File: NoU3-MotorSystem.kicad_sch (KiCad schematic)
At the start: 38 parts, among them J1 JST SR/SZ, J10 JST SR/SZ, J13 JST SR/SZ, J15 Barrel_Jack, J16 VIN, J17 JST SR/SZ, J18 GND, J4 JST SR/SZ, J7 JST SR/SZ, Q1 AO3401A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

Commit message: updated labels
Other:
- moved on the sheet: TP5
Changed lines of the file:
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@@
 	)
 	(junction
-		(at 72.39 140.97)
+		(at 166.37 40.64)
 		(diameter 0)
 		(color 0 0 0 0)
 	)
 	(junction
-		(at 59.69 171.45)
+		(at 72.39 140.97)
 		(diameter 0)
 		(color 0 0 0 0)
 	)
 	(junction
-		(at 68.58 109.22)
+		(at 59.69 171.45)
 		(diameter 0)
 		(color 0 0 0 0)
 	)
 	(junction
-		(at 166.37 35.56)
+		(at 68.58 109.22)
 		(diameter 0)
 		(color 0 0 0 0)
@@
 	)
 	(junction
-		(at 215.9 36.83)
-		(diameter 0)
-		(color 0 0 0 0)
-	)
-	(junction
 		(at 59.69 116.84)
 		(diameter 0)
@@
 	(wire
 		(pts
-			(xy 215.9 36.83) (xy 224.79 36.83)
-		)
-		(stroke
-			(width 0)
-			(type default)
-		)
-	)
-	(wire
-		(pts
 			(xy 189.23 116.84) (xy 198.12 116.84)
 		)
@@
 	(wire
 		(pts
-			(xy 224.79 35.56) (xy 166.37 35.56)
-		)
-		(stroke
-			(width 0)
-			(type default)
-		)
-	)
-	(wire
-		(pts
 			(xy 186.69 95.25) (xy 186.69 109.22)
 		)
@@
 	(wire
 		(pts
+			(xy 166.37 36.83) (xy 198.12 36.83)
+		)
+		(stroke
+			(width 0)
+			(type default)
+		)
+	)
+	(wire
+		(pts
 			(xy 128.27 104.14) (xy 120.65 104.14)
 		)
@@
 	(wire
 		(pts
-			(xy 181.61 71.12) (xy 181.61 96.52)
+			(xy 166.37 40.64) (xy 166.37 81.28)
 		)
 		(stroke
@@
 	(wire
 		(pts
-			(xy 186.69 116.84) (xy 163.83 116.84)
+			(xy 181.61 71.12) (xy 181.61 96.52)
 		)
 		(stroke
@@
 	(wire
 		(pts
-			(xy 198.12 66.04) (xy 179.07 66.04)
+			(xy 186.69 116.84) (xy 163.83 116.84)
 		)
 		(stroke
@@
 	(wire
 		(pts
-			(xy 191.77 111.76) (xy 191.77 121.92)
+			(xy 198.12 66.04) (xy 179.07 66.04)
 		)
 		(stroke
@@
 	(wire
 		(pts
-			(xy 43.18 124.46) (xy 59.69 124.46)
+			(xy 191.77 111.76) (xy 191.77 121.92)
 		)
 		(stroke
@@
 	(wire
 		(pts
-			(xy 48.26 163.83) (xy 59.69 163.83)
+			(xy 43.18 124.46) (xy 59.69 124.46)
 		)
 		(stroke
@@
 	(wire
 		(pts
-			(xy 166.37 35.56) (xy 166.37 81.28)
+			(xy 48.26 163.83) (xy 59.69 163.83)
 		)
 		(stroke
@@
 	(wire
 		(pts
-			(xy 224.79 36.83) (xy 224.79 35.56)
-		)
-		(stroke
-			(width 0)
-			(type default)
-		)
-	)
-	(wire
-		(pts
 			(xy 143.51 127) (xy 146.05 127)
 		)
@@
 	(wire
 		(pts
-			(xy 198.12 36.83) (xy 215.9 36.83)
+			(xy 48.26 140.97) (xy 59.69 140.97)
 		)
 		(stroke
@@
 	(wire
 		(pts
-			(xy 48.26 140.97) (xy 59.69 140.97)
+			(xy 260.35 124.46) (xy 255.27 124.46)
 		)
 		(stroke
@@
 	(wire
 		(pts
-			(xy 260.35 124.46) (xy 255.27 124.46)
+			(xy 60.96 116.84) (xy 59.69 116.84)
 		)
 		(stroke
@@
 	(wire
 		(pts
-			(xy 60.96 116.84) (xy 59.69 116.84)
+			(xy 85.09 140.97) (xy 90.17 140.97)
 		)
 		(stroke
@@
 	(wire
 		(pts
-			(xy 85.09 140.97) (xy 90.17 140.97)
+			(xy 198.12 31.75) (xy 173.99 31.75)
 		)
 		(stroke
@@
 	(wire
 		(pts
-			(xy 198.12 31.75) (xy 173.99 31.75)
+			(xy 115.57 73.66) (xy 115.57 88.9)
 		)
 		(stroke
@@
 	(wire
 		(pts
-			(xy 115.57 73.66) (xy 115.57 88.9)
+			(xy 166.37 36.83) (xy 166.37 40.64)
 		)
 		(stroke
@@
 	(symbol
 		(lib_id "Connector:TestPoint")
-		(at 166.37 35.56 90)
+		(at 166.37 40.64 90)
 		(unit 1)
 		(exclude_from_sim no)
@@
 		(dnp no)
 		(property "Reference" "TP5"
-			(at 161.29 35.56 90)
+			(at 161.29 40.64 90)
 			(effects
 				(font
@@
 		)
 		(property "Value" "LED0"
-			(at 161.29 33.02 90)
+			(at 161.29 38.1 90)
 			(effects
 				(font
@@
 		)
 		(property "Footprint" "AlfredoFootprints:PogoPad1"
-			(at 166.37 30.48 0)
+			(at 166.37 35.56 0)
 			(effects
 				(font
@@
 		)
 		(property "Datasheet" "~"
-			(at 166.37 30.48 0)
+			(at 166.37 35.56 0)
 			(effects
 				(font
@@
 		)
 		(property "Description" ""
-			(at 166.37 35.56 0)
+			(at 166.37 40.64 0)
 			(effects
 				(font
@@
 		)
 		(property "LCSC" "~"
-			(at 166.37 35.56 0)
+			(at 166.37 40.64 0)
 			(effects
 				(font

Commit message: updated for kicad 9
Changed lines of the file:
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@@
 (kicad_sch
-	(version 20231120)
+	(version 20250114)
 	(generator "eeschema")
-	(generator_version "8.0")
+	(generator_version "9.0")
 	(paper "A4")
+	(text "Power"
+		(exclude_from_sim no)
+		(at 24.13 104.14 0)
+		(effects
+			(font
+				(size 2.54 2.54)
+				(thickness 0.254)
+				(bold yes)
+			)
+			(justify left bottom)
+		)
+	)
+	(text "s"
+		(exclude_from_sim no)
+		(at 63.5 107.95 0)
+		(effects
+			(font
+				(size 1.27 1.27)
+				(bold yes)
+			)
+			(justify left bottom)
+		)
+	)
+	(text "d"
+		(exclude_from_sim no)
+		(at 52.07 107.95 0)
+		(effects
+			(font
+				(size 1.27 1.27)
+				(bold yes)
+			)
+			(justify left bottom)
+		)
+	)
+	(text "g\n"
+		(exclude_from_sim no)
+		(at 55.88 114.3 0)
+		(effects
+			(font
+				(size 1.27 1.27)
+				(bold yes)
+			)
+			(justify left bottom)
+		)
+	)
 	(junction
 		(at 30.48 168.91)
@@
 		)
 	)
-	(text "Power"
-		(exclude_from_sim no)
-		(at 24.13 104.14 0)
-		(effects
-			(font
-				(size 2.54 2.54)
-				(thickness 0.254)
-				(bold yes)
-			)
-			(justify left bottom)
-		)
-	)
-	(text "s"
-		(exclude_from_sim no)
-		(at 63.5 107.95 0)
-		(effects
-			(font
-				(size 1.27 1.27)
-				(bold yes)
-			)
-			(justify left bottom)
-		)
-	)
-	(text "d"
-		(exclude_from_sim no)
-		(at 52.07 107.95 0)
-		(effects
-			(font
-				(size 1.27 1.27)
-				(bold yes)
-			)
-			(justify left bottom)
-		)
-	)
-	(text "g\n"
-		(exclude_from_sim no)
-		(at 55.88 114.3 0)
-		(effects
-			(font
-				(size 1.27 1.27)
-				(bold yes)
-			)
-			(justify left bottom)
-		)
-	)
 	(global_label "E1B"
 		(shape input)
@@
 		(at 198.12 29.21)
 		(size 17.78 20.32)
+		(exclude_from_sim no)
+		(in_bom yes)
+		(on_board yes)
+		(dnp no)
 		(fields_autoplaced yes)
 		(stroke
@@
 		(at 198.12 87.63)
 		(size 17.78 20.32)
+		(exclude_from_sim no)
+		(in_bom yes)
+		(on_board yes)
+		(dnp no)
 		(fields_autoplaced yes)
 		(stroke
@@
 		(at 198.12 114.3)
 		(size 17.78 20.32)
+		(exclude_from_sim no)
+		(in_bom yes)
+		(on_board yes)
+		(dnp no)
 		(fields_autoplaced yes)
 		(stroke
@@
 		(at 198.12 60.96)
 		(size 17.78 20.32)
+		(exclude_from_sim no)
+		(in_bom yes)
+		(on_board yes)
+		(dnp no)
 		(fields_autoplaced yes)
 		(stroke

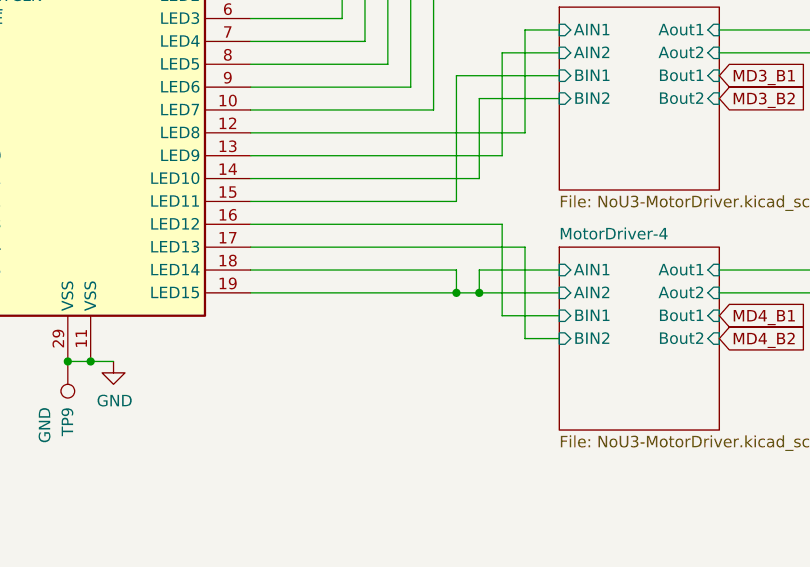
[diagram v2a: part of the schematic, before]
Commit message: Update wiring and remove unused junctions in schematic
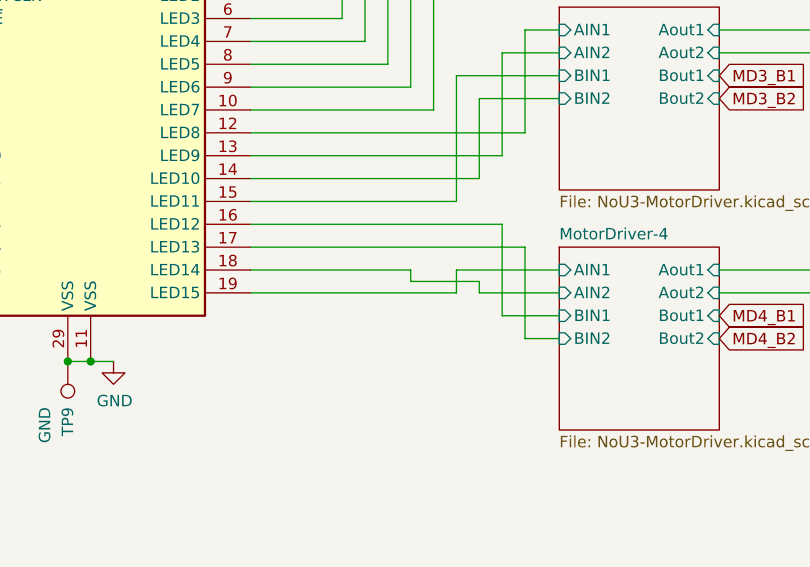
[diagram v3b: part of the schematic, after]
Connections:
- net MotorDriver-4/AIN1: no longer U10.18 (LED14)
- new net MotorDriver-4/AIN2: U10.18 (LED14)
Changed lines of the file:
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@@
-	)
-	(junction
-		(at 186.69 119.38)
-		(diameter 0)
-		(color 0 0 0 0)
 	)
 	(junction
@@
 	)
 	(junction
-		(at 189.23 119.38)
-		(diameter 0)
-		(color 0 0 0 0)
-	)
-	(junction
 		(at 30.48 133.35)
 		(diameter 0)
@@
 	(wire
 		(pts
+			(xy 163.83 116.84) (xy 181.61 116.84)
+		)
+		(stroke
+			(width 0)
+			(type default)
+		)
+	)
+	(wire
+		(pts
 			(xy 215.9 116.84) (xy 232.41 116.84)
 		)
@@
 	(wire
 		(pts
+			(xy 189.23 119.38) (xy 189.23 118.11)
+		)
+		(stroke
+			(width 0)
+			(type default)
+		)
+	)
+	(wire
+		(pts
 			(xy 45.72 106.68) (xy 45.72 109.22)
 		)
@@
 	(wire
 		(pts
-			(xy 189.23 116.84) (xy 198.12 116.84)
-		)
-		(stroke
-			(width 0)
-			(type default)
-		)
-	)
-	(wire
-		(pts
 			(xy 30.48 148.59) (xy 39.37 148.59)
 		)
@@
 	(wire
 		(pts
+			(xy 186.69 116.84) (xy 198.12 116.84)
+		)
+		(stroke
+			(width 0)
+			(type default)
+		)
+	)
+	(wire
+		(pts
 			(xy 59.69 171.45) (xy 62.23 171.45)
 		)
@@
 	(wire
 		(pts
+			(xy 189.23 118.11) (xy 181.61 118.11)
+		)
+		(stroke
+			(width 0)
+			(type default)
+		)
+	)
+	(wire
+		(pts
 			(xy 215.9 90.17) (xy 232.41 90.17)
 		)
@@
 	(wire
 		(pts
+			(xy 163.83 119.38) (xy 186.69 119.38)
+		)
+		(stroke
+			(width 0)
+			(type default)
+		)
+	)
+	(wire
+		(pts
 			(xy 69.85 109.22) (xy 72.39 109.22)
 		)
@@
 	(wire
 		(pts
+			(xy 186.69 119.38) (xy 186.69 116.84)
+		)
+		(stroke
+			(width 0)
+			(type default)
+		)
+	)
+	(wire
+		(pts
 			(xy 229.87 121.92) (xy 232.41 121.92)
 		)
@@
 	(wire
 		(pts
-			(xy 163.83 119.38) (xy 186.69 119.38)
-		)
-		(stroke
-			(width 0)
-			(type default)
-		)
-	)
-	(wire
-		(pts
 			(xy 166.37 36.83) (xy 198.12 36.83)
 		)
@@
 	(wire
 		(pts
-			(xy 186.69 119.38) (xy 186.69 116.84)
-		)
-		(stroke
-			(width 0)
-			(type default)
-		)
-	)
-	(wire
-		(pts
 			(xy 80.01 179.07) (xy 72.39 179.07)
 		)
@@
 	(wire
 		(pts
-			(xy 186.69 116.84) (xy 163.83 116.84)
-		)
-		(stroke
-			(width 0)
-			(type default)
-		)
-	)
-	(wire
-		(pts
 			(xy 198.12 66.04) (xy 179.07 66.04)
 		)
@@
 	(wire
 		(pts
-			(xy 189.23 119.38) (xy 189.23 116.84)
-		)
-		(stroke
-			(width 0)
-			(type default)
-		)
-	)
-	(wire
-		(pts
 			(xy 232.41 41.91) (xy 223.52 41.91)
 		)
@@
 	(wire
 		(pts
+			(xy 181.61 118.11) (xy 181.61 116.84)
+		)
+		(stroke
+			(width 0)
+			(type default)
+		)
+	)
+	(wire
+		(pts
 			(xy 24.13 179.07) (xy 30.48 179.07)
 		)
@@
 		)
 		(stroke
-			(width 0)
-			(type default)
-		)
-	)
-	(wire
-		(pts
-			(xy 186.69 119.38) (xy 189.23 119.38)
-		)
-		(stroke

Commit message: bumped version to NoU3.5
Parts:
- U10: LCSC (none) -> C5191634
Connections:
- net M_ECLK: now reaches TP4.1, U10.22 (EXTCLK)
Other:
- moved on the sheet: TP4
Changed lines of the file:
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@@
 	)
 	(junction
+		(at 110.49 86.36)
+		(diameter 0)
+		(color 0 0 0 0)
+	)
+	(junction
 		(at 30.48 168.91)
 		(diameter 0)
@@
 	(wire
 		(pts
-			(xy 113.03 88.9) (xy 115.57 88.9)
+			(xy 101.6 88.9) (xy 115.57 88.9)
 		)
 		(stroke
@@
 	(wire
 		(pts
+			(xy 110.49 91.44) (xy 110.49 86.36)
+		)
+		(stroke
+			(width 0)
+			(type default)
+		)
+	)
+	(wire
+		(pts
 			(xy 168.91 83.82) (xy 163.83 83.82)
 		)
@@
 	(wire
 		(pts
+			(xy 110.49 86.36) (xy 128.27 86.36)
+		)
+		(stroke
+			(width 0)
+			(type default)
+		)
+	)
+	(wire
+		(pts
 			(xy 215.9 92.71) (xy 232.41 92.71)
 		)
@@
 	(wire
 		(pts
-			(xy 113.03 81.28) (xy 125.73 81.28)
+			(xy 101.6 81.28) (xy 125.73 81.28)
 		)
 		(stroke
@@
 	(wire
 		(pts
+			(xy 101.6 86.36) (xy 110.49 86.36)
+		)
+		(stroke
+			(width 0)
+			(type default)
+		)
+	)
+	(wire
+		(pts
 			(xy 143.51 73.66) (xy 146.05 73.66)
 		)
@@
 	(wire
 		(pts
-			(xy 113.03 83.82) (xy 120.65 83.82)
+			(xy 101.6 83.82) (xy 120.65 83.82)
 		)
 		(stroke
@@
 	(wire
 		(pts
-			(xy 113.03 86.36) (xy 128.27 86.36)
-		)
-		(stroke
-			(width 0)
-			(type default)
-		)
-	)
-	(wire
-		(pts
 			(xy 48.26 171.45) (xy 59.69 171.45)
 		)
@@
 	(global_label "SF_SDA"
 		(shape input)
-		(at 113.03 83.82 180)
+		(at 101.6 83.82 180)
 		(fields_autoplaced yes)
 		(effects
@@
 		)
 		(property "Intersheetrefs" "${INTERSHEET_REFS}"
-			(at 103.9446 83.82 0)
+			(at 92.5146 83.82 0)
 			(effects
 				(font
@@
 	(global_label "SF_SCL"
 		(shape input)
-		(at 113.03 81.28 180)
+		(at 101.6 81.28 180)
 		(fields_autoplaced yes)
 		(effects
@@
 		)
 		(property "Intersheetrefs" "${INTERSHEET_REFS}"
-			(at 104.0051 81.28 0)
+			(at 92.5751 81.28 0)
 			(effects
 				(font
@@
 		)
 	)
+	(global_label "M_ECLK"
+		(shape input)
+		(at 101.6 86.36 180)
+		(fields_autoplaced yes)
+		(effects
+			(font
+				(size 1.27 1.27)
+			)
+			(justify right)
+		)
+		(property "Intersheetrefs" "${INTERSHEET_REFS}"
+			(at 92.1329 86.36 0)
+			(effects
+				(font
+					(size 1.27 1.27)
+				)
+				(justify right)
+				(hide yes)
+			)
+		)
+	)
 	(global_label "M_OE"
 		(shape input)
-		(at 113.03 88.9 180)
+		(at 101.6 88.9 180)
 		(fields_autoplaced yes)
 		(effects
@@
 		)
 		(property "Intersheetrefs" "${INTERSHEET_REFS}"
-			(at 105.8005 88.9 0)
+			(at 94.3705 88.9 0)
 			(effects
 				(font
@@
 	(symbol
 		(lib_id "Connector:TestPoint")
-		(at 113.03 86.36 90)
+		(at 110.49 91.44 180)
 		(unit 1)
 		(exclude_from_sim no)
@@
 		(dnp no)
 		(property "Reference" "TP4"
-			(at 102.87 86.36 90)
+			(at 108.458 96.774 90)
 			(effects
 				(font
@@
 		)
 		(property "Value" "ECLK"
-			(at 108.458 86.36 90)
+			(at 110.49 96.012 90)
 			(effects
 				(font
@@
 		)
 		(property "Footprint" "AlfredoFootprints:PogoPad1"
-			(at 113.03 81.28 0)
+			(at 105.41 91.44 0)
 			(effects
 				(font
@@
 		)
 		(property "Datasheet" "~"
-			(at 113.03 81.28 0)
+			(at 105.41 91.44 0)
 			(effects
 				(font
@@
 		)
 		(property "Description" ""
-			(at 113.03 86.36 0)
+			(at 110.49 91.44 0)
 			(effects
 				(font
@@
 		)
 		(property "LCSC" "~"
-			(at 113.03 86.36 0)
+			(at 110.49 91.44 0)
 			(effects
 				(font
@@
 			)
 		)
+		(property "LCSC" " C5191634"
+			(at 146.05 99.06 0)
+			(effects
+				(font
+					(size 1.27 1.27)
+				)
+			)
+		)

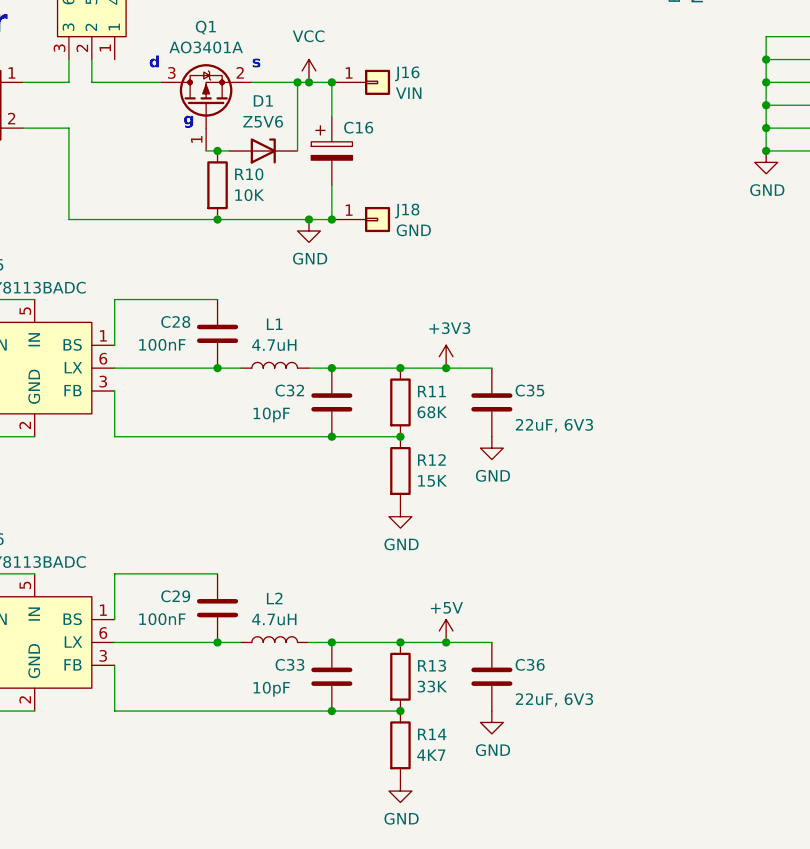
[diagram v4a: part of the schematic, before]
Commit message: removed mag sensor, improved regulator resistor values
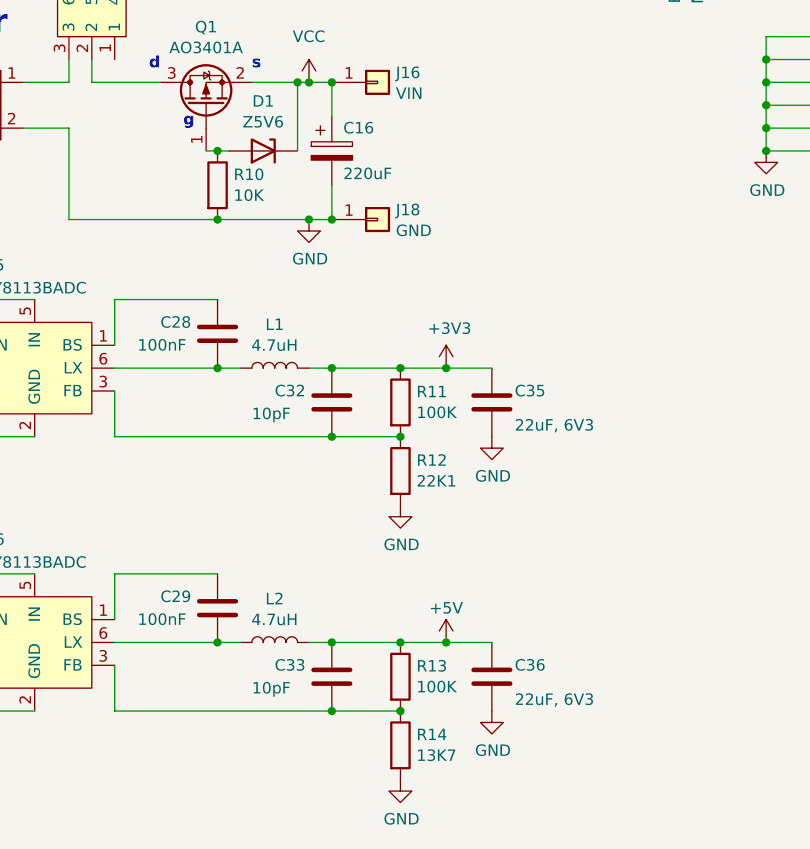
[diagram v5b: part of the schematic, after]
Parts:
- C16: value ~ -> 220uF
- R11: value 68K -> 100K; LCSC C36871 -> (none)
- R12: value 15K -> 22K1; LCSC C25756 -> C163478
- R13: value 33K -> 100K; LCSC C25779 -> C25741
- R14: value 4K7 -> 13K7; LCSC C25900 -> C25854
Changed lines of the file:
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@@
 			)
 		)
-		(property "Value" "4K7"
+		(property "Value" "13K7"
 			(at 81.788 184.023 0)
 			(effects
@@
 			)
 		)
-		(property "Datasheet" "https://www.lcsc.com/product-detail/Chip-Resistor---Surface-Mount_UNI-ROYALUniroyal-Elec-UNI-ROYALUniroyal-Elec-0402WGF4701TCE_C25900.html"
+		(property "Datasheet" ""
 			(at 80.01 182.88 0)
 			(effects
@@
 			)
 		)
-		(property "LCSC" "C25900"
+		(property "LCSC" "C25854"
 			(at 80.01 182.88 0)
 			(effects
@@
 			)
 		)
-		(property "Value" "~"
+		(property "Value" "220uF"
 			(at 73.66 119.38 0)
 			(effects
@@
 			)
 		)
-		(property "Value" "15K"
+		(property "Value" "22K1"
 			(at 81.788 153.543 0)
 			(effects
@@
 			)
 		)
-		(property "Datasheet" "https://lcsc.com/product-detail/Chip-Resistor---Surface-Mount_UNI-ROYALUniroyal-Elec-UNI-ROYALUniroyal-Elec-0402WGF1502TCE_C25756.html"
+		(property "Datasheet" ""
 			(at 80.01 152.4 0)
 			(effects
@@
 			)
 		)
-		(property "LCSC" "C25756"
+		(property "LCSC" "C163478 "
 			(at 80.01 152.4 0)
 			(effects
@@
 			)
 		)
-		(property "Value" "68K"
+		(property "Value" "100K"
 			(at 81.788 145.923 0)
 			(effects
@@
 			)
 		)
-		(property "Datasheet" "https://lcsc.com/product-detail/Chip-Resistor---Surface-Mount_UNI-ROYALUniroyal-Elec-UNI-ROYALUniroyal-Elec-0402WGF6802TCE_C36871.html"
+		(property "Datasheet" ""
 			(at 80.01 144.78 0)
 			(effects
@@
 			)
 		)
-		(property "LCSC" "C36871"
+		(property "LCSC" ""
 			(at 80.01 144.78 0)
 			(effects
@@
 			)
 		)
-		(property "Value" "33K"
+		(property "Value" "100K"
 			(at 81.788 176.403 0)
 			(effects
@@
 			)
 		)
-		(property "Datasheet" "https://www.lcsc.com/product-detail/Chip-Resistor---Surface-Mount_UNI-ROYALUniroyal-Elec-UNI-ROYALUniroyal-Elec-0402WGF3302TCE_C25779.html"
+		(property "Datasheet" ""
 			(at 80.01 175.26 0)
 			(effects
@@
 			)
 		)
-		(property "LCSC" "C25779"
+		(property "LCSC" "C25741"
 			(at 80.01 175.26 0)
 			(effects
